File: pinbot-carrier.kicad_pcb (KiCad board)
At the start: 2 copper layers, 150 x 30 mm, 118 parts, among them J1 USB4105-GF-A-120, J2 Conn_02x20_Odd_Even, J3 HC-1.0-4PWT, J4 SM06B-SRSS-TB, J5 USB_A, J6 USB_A, J7 USB_A, K1 EC2-5SNU, K2 EC2-5SNU, K3 EC2-5SNU, K4 EC2-5SNU, U1 TCA9535PWR, U10 ZXBM5210-S, U11 ZXBM5210-S, U12 ZXBM5210-S, U13 MIC2026-2xM, U14 USBLC6-2SC6, U15 USBLC6-2SC6, U16 USBLC6-2SC6, U17 USBLC6-2SC6, U18 FE1.1s, U19 MIC2026-2xM, U2 ADS1015IDGS, U7 ADS1015IDGS, U8 74HC04, U9 ZXBM5210-S, Y1 12MHz

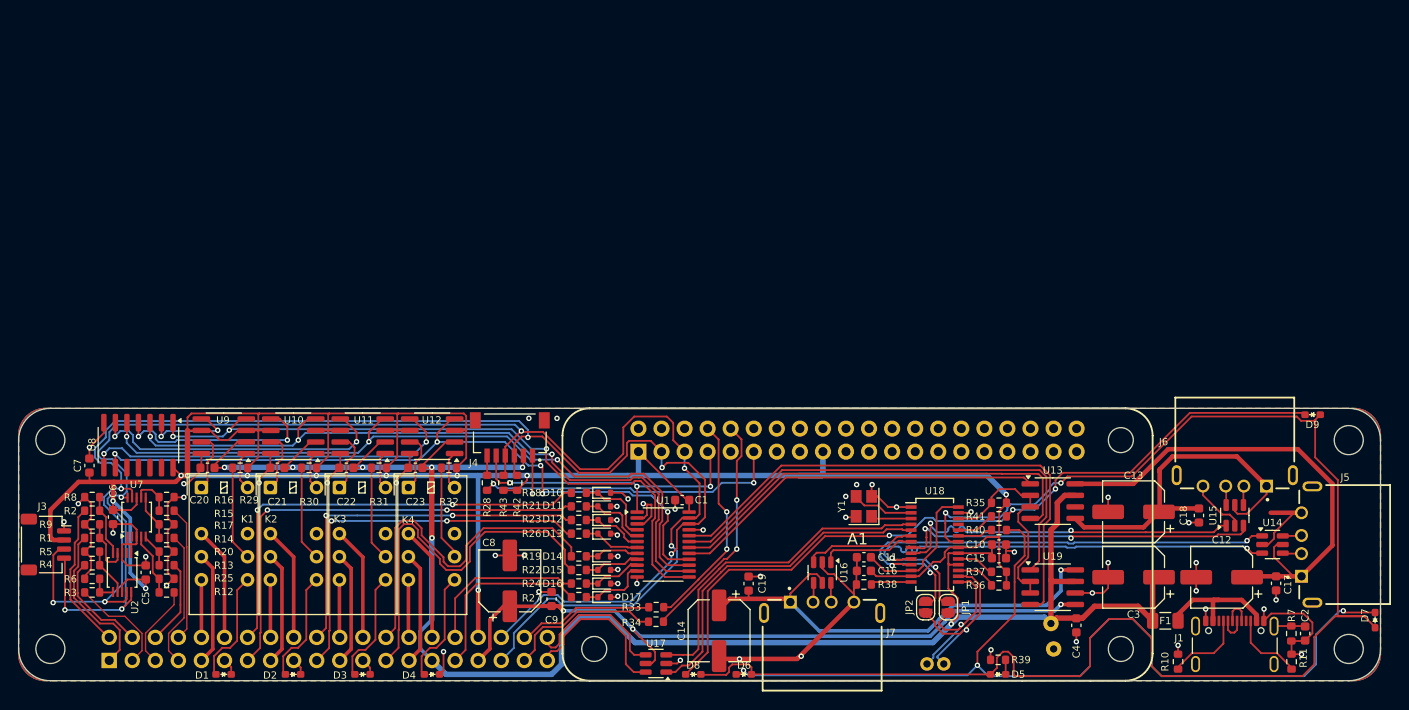
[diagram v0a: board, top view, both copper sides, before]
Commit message: r0.2 remade from a scratch
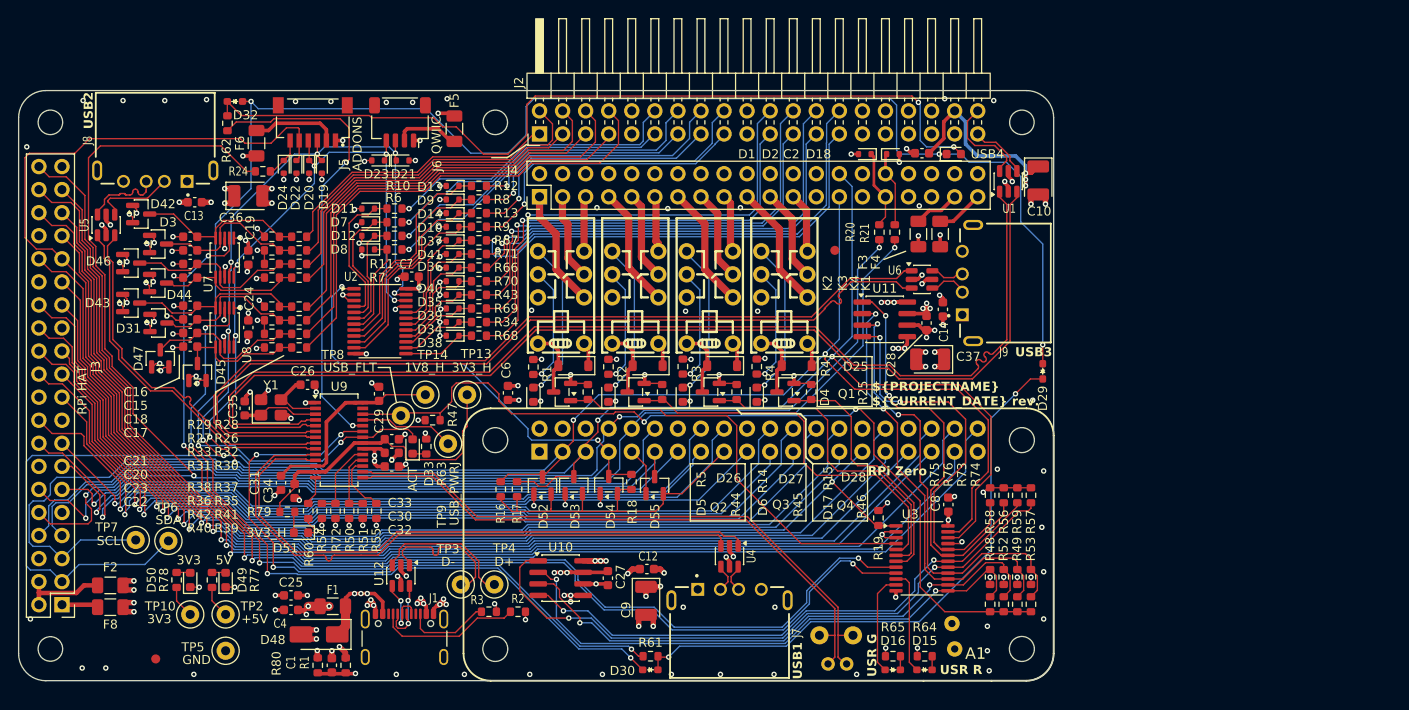
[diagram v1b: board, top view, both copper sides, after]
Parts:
- removed C11: 10uFx10V, Capacitor_SMD:C_0603_1608Metric
- removed the C13 at (122.8, -18.6)
- removed the C14 at (77.2, -5.50)
- removed C3: 100uFx16V, Capacitor_SMD:CP_Elec_6.3x5.4
- removed C5: 0.1uFx50V, Capacitor_SMD:C_0603_1608Metric
- removed the C7 at (7.80, -23.7)
- removed the C9 at (58.7, -9.00)
- removed JP1, JP2: SolderJumper_2_Open, Jumper:SolderJumper-2_P1.3mm_Open_RoundedPad1.0x1.5mm
- removed the R1 at (8.10, -15.7)
- removed the R16 at (16.3, -20.2)
- removed the R17 at (16.3, -17.2)
- removed the R2 at (8.10, -18.7)
- removed the R20 at (16.3, -14.2)
- removed the R21 at (61.7, -19.2)
- removed R22, R23: 10k, Resistor_SMD:R_0603_1608Metric
- removed the R24 at (61.7, -10.7)
- removed the R3 at (8.10, -9.72)
- removed U13, U19: MIC2026-2xM, Package_SO:SOIC-8_3.9x4.9mm_P1.27mm
- removed U18: FE1.1s, Package_SO:SSOP-28_3.9x9.9mm_P0.635mm
- removed the U2 at (11.4, -11.9)
- added C17: 0.1uFx50V, Capacitor_SMD:C_0603_1608Metric, F.Cu at (18.9, -44.4)
- added C18: 0.1uFx50V, Capacitor_SMD:C_0603_1608Metric, F.Cu at (18.9, -45.9)
- added C19: 0.1uFx50V, Capacitor_SMD:C_0603_1608Metric, F.Cu at (25.3, -46.6)
- added C2: 0.1uFx50V, Capacitor_SMD:C_0603_1608Metric, F.Cu at (99.5, -58.1)
- added C24: 0.1uFx50V, Capacitor_SMD:C_0603_1608Metric, F.Cu at (25.3, -38.9)
- added C25: 10uFx10V, Capacitor_SMD:C_0603_1608Metric, F.Cu at (30.0, -9.40)
- added C26: 14pFx50V, Capacitor_SMD:C_0603_1608Metric, F.Cu at (31.8, -32.6)
- added C27: 0.1uFx50V, Capacitor_SMD:C_0603_1608Metric, F.Cu at (64.9, -11.3)
- added C28: 0.1uFx50V, Capacitor_SMD:C_0603_1608Metric, F.Cu at (100.0, -39.4)
- added C29: 0.1uFx50V, Capacitor_SMD:C_0603_1608Metric, F.Cu at (39.7, -31.6)
- added C30: 0.1uFx50V, Capacitor_SMD:C_0603_1608Metric, F.Cu at (41.1, -25.1)
- added C31: 10uFx10V, Capacitor_SMD:C_0603_1608Metric, F.Cu at (28.9, -21.8)
- added C32: 10uFx10V, Capacitor_SMD:C_0603_1608Metric, F.Cu at (41.1, -23.6)
- added C33: 10uFx10V, Capacitor_SMD:C_0603_1608Metric, F.Cu at (41.1, -26.6)
- added C34: 0.1uFx50V, Capacitor_SMD:C_0603_1608Metric, F.Cu at (30.4, -20.9)
- added C35: 14pFx50V, Capacitor_SMD:C_0603_1608Metric, F.Cu at (24.9, -30.0)
- added C36: 100uFx10V, Capacitor_Tantalum_SMD:CP_EIA-3528-21_Kemet-B, F.Cu at (25.3, -53.4)
- added C37: 100uFx10V, Capacitor_Tantalum_SMD:CP_EIA-3528-21_Kemet-B, F.Cu at (100.4, -35.4)
- added D18: 19-21/GHC-YR1S2/4T, LED_SMD:LED_0603_1608Metric, F.Cu at (103.0, -58.0)
- added D19: ESD5Z3.3T5G, Diode_SMD:D_SOD-523, F.Cu at (33.4, -56.6)
- added D20: ESD5Z3.3T5G, Diode_SMD:D_SOD-523, F.Cu at (32.0, -56.6)
- added D21: ESD5Z3.3T5G, Diode_SMD:D_SOD-523, F.Cu at (42.3, -57.3)
- added D22: ESD5Z3.3T5G, Diode_SMD:D_SOD-523, F.Cu at (30.6, -56.6)
- added D23: ESD5Z3.3T5G, Diode_SMD:D_SOD-523, F.Cu at (39.6, -57.3)
- added D24: ESD5Z3.3T5G, Diode_SMD:D_SOD-523, F.Cu at (29.2, -56.6)
- added D25: MMSD4148, Diode_SMD:D_SOD-123, F.Cu at (85.7, -34.7)
- added D26: MMSD4148, Diode_SMD:D_SOD-123, F.Cu at (61.1, -34.7)
- added D27: MMSD4148, Diode_SMD:D_SOD-123, F.Cu at (69.3, -34.7)
- added D28: MMSD4148, Diode_SMD:D_SOD-123, F.Cu at (77.5, -34.7)
- added D29: LTST-S270KGKT, LED_0603_1608Metric_side:LED_0603_1608Metric_side, F.Cu at (112.8, -34.1)
- added D30: LTST-S270KGKT, LED_0603_1608Metric_side:LED_0603_1608Metric_side, F.Cu at (69.6, -1.20)
- added D31: BAT54S, Package_TO_SOT_SMD:SOT-23, F.Cu at (15.4, -39.4)
- added D32: LTST-S270KGKT, LED_0603_1608Metric_side:LED_0603_1608Metric_side, F.Cu at (23.8, -63.8)
- added D33: XL-1608SURC-06, LED_SMD:LED_0603_1608Metric, F.Cu at (43.4, -25.8)
- added D34: ESD5Z3.3T5G, Diode_SMD:D_SOD-523, F.Cu at (47.8, -39.5)
- added D35: ESD5Z3.3T5G, Diode_SMD:D_SOD-523, F.Cu at (47.8, -42.5)
- added D36: ESD5Z3.3T5G, Diode_SMD:D_SOD-523, F.Cu at (47.8, -45.5)
- added D37: ESD5Z3.3T5G, Diode_SMD:D_SOD-523, F.Cu at (47.8, -48.5)
- added D38: ESD5Z3.3T5G, Diode_SMD:D_SOD-523, F.Cu at (47.8, -38.0)
- added D39: ESD5Z3.3T5G, Diode_SMD:D_SOD-523, F.Cu at (47.8, -41.0)
- added D40: ESD5Z3.3T5G, Diode_SMD:D_SOD-523, F.Cu at (47.8, -44.0)
- added D41: ESD5Z3.3T5G, Diode_SMD:D_SOD-523, F.Cu at (47.8, -47.0)
- added D42: BAT54S, Package_TO_SOT_SMD:SOT-23, F.Cu at (13.5, -51.4)
- added D43: BAT54S, Package_TO_SOT_SMD:SOT-23, F.Cu at (12.4, -41.6)
- added D44: BAT54S, Package_TO_SOT_SMD:SOT-23, F.Cu at (15.4, -43.8)
- added D45: BAT54S, Package_TO_SOT_SMD:SOT-23, F.Cu at (19.7, -34.0)
- added D46: BAT54S, Package_TO_SOT_SMD:SOT-23, F.Cu at (12.4, -46.0)
- added D47: BAT54S, Package_TO_SOT_SMD:SOT-23, F.Cu at (15.6, -35.5)
- added D48: SMAJ5.0A, Diode_SMD:D_SMA, F.Cu at (33.1, -5.10)
- added D49: XL-1608SURC-06, LED_SMD:LED_0603_1608Metric, F.Cu at (22.8, -11.1)
- added D50: XL-1608SURC-06, LED_SMD:LED_0603_1608Metric, F.Cu at (18.9, -11.1)
- added D51: XL-1608SURC-06, LED_SMD:LED_0603_1608Metric, F.Cu at (31.1, -16.3)
- added D52: BAT54S, Package_TO_SOT_SMD:SOT-23, F.Cu at (57.7, -21.5)
- added D53: BAT54S, Package_TO_SOT_SMD:SOT-23, F.Cu at (61.1, -21.5)
- added D54: BAT54S, Package_TO_SOT_SMD:SOT-23, F.Cu at (65.0, -21.6)
- added D55: BAT54S, Package_TO_SOT_SMD:SOT-23, F.Cu at (70.0, -21.5)
- added F2: MF-NSMF110-2, Fuse:Fuse_1206_3216Metric, F.Cu at (10.1, -10.5)
- added F3: MF-NSMF110-2, Fuse:Fuse_1206_3216Metric, F.Cu at (99.1, -49.2)
- added F4: MF-NSMF110-2, Fuse:Fuse_1206_3216Metric, F.Cu at (101.5, -49.2)
- added F5: MF-NSMF110-2, Fuse:Fuse_1206_3216Metric, F.Cu at (48.0, -60.8)
- added F6: MF-NSMF110-2, Fuse:Fuse_1206_3216Metric, F.Cu at (26.2, -59.2)
- added F8: MF-NSMF110-2, Fuse:Fuse_1206_3216Metric, F.Cu at (10.1, -8.10)
- added FID1: Fiducial, Fiducial:Fiducial_1mm_Mask2mm, F.Cu at (15.1, -2.40)
- added FID2: Fiducial, Fiducial:Fiducial_1mm_Mask2mm, F.Cu at (89.9, -47.4)
- added J5: SM06B-SRSS-TB, SM06B-SRSS-TB:JST_SM06B-SRSS-TB, F.Cu at (32.4, -59.5)
- added J6: HC-1.0-4PWT, Connector_JST:JST_SH_SM04B-SRSS-TB_1x04-1MP_P1.00mm_Horizontal, F.Cu at (42.0, -61.5)
- added Q1: 2N7002, Package_TO_SOT_SMD:SOT-23, F.Cu at (84.5, -31.8)
- added Q2: 2N7002, Package_TO_SOT_SMD:SOT-23, F.Cu at (59.9, -31.8)
- added Q3: 2N7002, Package_TO_SOT_SMD:SOT-23, F.Cu at (68.0, -31.8)
- added Q4: 2N7002, Package_TO_SOT_SMD:SOT-23, F.Cu at (76.2, -31.8)
- added R10: 10k, Resistor_SMD:R_0603_1608Metric, F.Cu at (41.4, -52.0)
- added R11: 10k, Resistor_SMD:R_0603_1608Metric, F.Cu at (41.4, -49.0)
- added R28: 110k, Resistor_SMD:R_0603_1608Metric, F.Cu at (30.9, -48.9)
- added R33: 10k, Resistor_SMD:R_0603_1608Metric, F.Cu at (27.9, -45.9)
- added R34: 10k, Resistor_SMD:R_0603_1608Metric, F.Cu at (50.7, -39.5)
- added R42: 10k, Resistor_SMD:R_0603_1608Metric, F.Cu at (27.9, -38.2)
- added R43: 10k, Resistor_SMD:R_0603_1608Metric, F.Cu at (50.7, -42.5)
- added R44: 10k, Resistor_SMD:R_0603_1608Metric, F.Cu at (62.7, -31.8)
- added R45: 10k, Resistor_SMD:R_0603_1608Metric, F.Cu at (70.9, -31.8)
- added R46: 10k, Resistor_SMD:R_0603_1608Metric, F.Cu at (79.1, -31.8)
- added R47: 10k, Resistor_SMD:R_0603_1608Metric, F.Cu at (45.6, -28.7)
- added R48: 330R, Resistor_SMD:R_0603_1608Metric, F.Cu at (107.0, -8.43)
- added R49: 330R, Resistor_SMD:R_0603_1608Metric, F.Cu at (110.0, -8.43)
- added R50: 51k, Resistor_SMD:R_0603_1608Metric, F.Cu at (36.4, -18.7)
- added R51: 51k, Resistor_SMD:R_0603_1608Metric, F.Cu at (37.9, -18.7)
- added R52: 330R, Resistor_SMD:R_0603_1608Metric, F.Cu at (108.5, -8.43)
- added R53: 330R, Resistor_SMD:R_0603_1608Metric, F.Cu at (111.5, -8.43)
- added R54: 10k, Resistor_SMD:R_0603_1608Metric, F.Cu at (33.4, -18.7)
- added R55: 10k, Resistor_SMD:R_0603_1608Metric, F.Cu at (39.4, -18.7)
- added R56: 10k, Resistor_SMD:R_0603_1608Metric, F.Cu at (108.5, -11.4)
- added R57: 10k, Resistor_SMD:R_0603_1608Metric, F.Cu at (111.5, -11.4)
- added R58: 10k, Resistor_SMD:R_0603_1608Metric, F.Cu at (107.0, -11.4)
- added R59: 10k, Resistor_SMD:R_0603_1608Metric, F.Cu at (110.0, -11.4)
- added R60: 2.7k, Resistor_SMD:R_0603_1608Metric, F.Cu at (31.9, -18.7)
- added R61: 330R, Resistor_SMD:R_0603_1608Metric, F.Cu at (69.6, -2.70)
- added R62: 330R, Resistor_SMD:R_0603_1608Metric, F.Cu at (23.0, -61.4)
- added R63: 330R, Resistor_SMD:R_0603_1608Metric, F.Cu at (44.9, -25.8)
- added R64: 330R, Resistor_SMD:R_0603_1608Metric, F.Cu at (99.8, -2.70)
- added R65: 330R, Resistor_SMD:R_0603_1608Metric, F.Cu at (96.3, -2.70)
- added R66: 10k, Resistor_SMD:R_0603_1608Metric, F.Cu at (50.7, -45.5)
- added R67: 10k, Resistor_SMD:R_0603_1608Metric, F.Cu at (50.7, -48.5)
- added R68: 10k, Resistor_SMD:R_0603_1608Metric, F.Cu at (50.7, -38.0)
- added R69: 10k, Resistor_SMD:R_0603_1608Metric, F.Cu at (50.7, -41.0)
- added R7: 10k, Resistor_SMD:R_0603_1608Metric, F.Cu at (41.4, -47.5)
- added R70: 10k, Resistor_SMD:R_0603_1608Metric, F.Cu at (50.7, -44.0)
- added R71: 10k, Resistor_SMD:R_0603_1608Metric, F.Cu at (50.7, -47.0)
- added R72: 10k, Resistor_SMD:R_0603_1608Metric, F.Cu at (34.9, -18.7)
- added R73: 10k, Resistor_SMD:R_0603_1608Metric, F.Cu at (110.0, -20.4)
- added R74: 10k, Resistor_SMD:R_0603_1608Metric, F.Cu at (111.5, -20.4)
- added R75: 10k, Resistor_SMD:R_0603_1608Metric, F.Cu at (107.0, -20.4)
- added R76: 10k, Resistor_SMD:R_0603_1608Metric, F.Cu at (108.5, -20.4)
- added R77: 330R, Resistor_SMD:R_0603_1608Metric, F.Cu at (21.3, -11.1)
- added R78: 330R, Resistor_SMD:R_0603_1608Metric, F.Cu at (17.4, -11.1)
- added R79: 330R, Resistor_SMD:R_0603_1608Metric, F.Cu at (29.6, -18.6)
- added R80: 0, Resistor_SMD:R_0603_1608Metric, F.Cu at (32.9, -1.70)
- added TP10: 3V3, JLCImport:TestPoint_Loop_D1.80mm_Drill1.0mm_Beaded, F.Cu at (18.9, -7.30)
- added TP11: RPI_D+, JLCImport:TestPoint_Loop_D1.80mm_Drill1.0mm_Beaded, B.Cu at (91.9, -5.00)
- added TP12: RPI_D-, JLCImport:TestPoint_Loop_D1.80mm_Drill1.0mm_Beaded, B.Cu at (88.2, -5.00)
- added TP13: 3V3_H, JLCImport:TestPoint_Loop_D1.80mm_Drill1.0mm_Beaded, F.Cu at (49.4, -31.5)
- added TP14: 1V8_H, JLCImport:TestPoint_Loop_D1.80mm_Drill1.0mm_Beaded, F.Cu at (44.8, -31.5)
- added TP2: +5V, JLCImport:TestPoint_Loop_D1.80mm_Drill1.0mm_Beaded, F.Cu at (22.8, -7.30)
- added TP3: D-, JLCImport:TestPoint_Loop_D1.80mm_Drill1.0mm_Beaded, F.Cu at (48.7, -10.6)
- added TP4: D+, JLCImport:TestPoint_Loop_D1.80mm_Drill1.0mm_Beaded, F.Cu at (52.4, -10.6)
- added TP5: GND, JLCImport:TestPoint_Loop_D1.80mm_Drill1.0mm_Beaded, F.Cu at (22.8, -3.30)
- added TP6: SDA, JLCImport:TestPoint_Loop_D1.80mm_Drill1.0mm_Beaded, F.Cu at (16.5, -15.4)
- added TP7: SCL, JLCImport:TestPoint_Loop_D1.80mm_Drill1.0mm_Beaded, F.Cu at (12.9, -15.5)
- added TP8: USB_FLT, JLCImport:TestPoint_Loop_D1.80mm_Drill1.0mm_Beaded, F.Cu at (42.1, -29.2)
- added TP9: USB_PWRJ, JLCImport:TestPoint_Loop_D1.80mm_Drill1.0mm_Beaded, F.Cu at (47.3, -26.1)
- added U3: TCA9535PWR, Package_SO:TSSOP-24_4.4x7.8mm_P0.65mm, F.Cu at (99.5, -13.5)
- C10: value 0.1uFx50V -> 100uFx10V; footprint Capacitor_SMD:C_0603_1608Metric -> Capacitor_Tantalum_SMD:CP_EIA-3528-21_Kemet-B
- C15, C16: value 10uFx10V -> 0.1uFx50V
- C6: value 0.1uFx50V -> 10uFx10V
- C8: value 100uFx16V -> 0.1uFx50V; footprint Capacitor_SMD:CP_Elec_6.3x5.4 -> Capacitor_SMD:C_0603_1608Metric
- C9: renamed from C12; value 100uFx16V -> 100uFx10V; footprint Capacitor_SMD:CP_Elec_6.3x5.4 -> Capacitor_Tantalum_SMD:CP_EIA-3528-21_Kemet-B
- D1, D2, D7, D8, D9: value LTST-S270KGKT -> ESD5Z3.3T5G; footprint LED_0603_1608Metric_side:LED_0603_1608Metric_side -> Diode_SMD:D_SOD-523
- D15: value ESD5Z3.3T5G -> LTST-S270KRKT; footprint Diode_SMD:D_SOD-523 -> LED_0603_1608Metric_side:LED_0603_1608Metric_side
- D16: value ESD5Z3.3T5G -> LTST-S270KGKT; footprint Diode_SMD:D_SOD-523 -> LED_0603_1608Metric_side:LED_0603_1608Metric_side
- D17: value ESD5Z3.3T5G -> 19-21/GHC-YR1S2/4T; footprint Diode_SMD:D_SOD-523 -> LED_SMD:LED_0603_1608Metric
- D3: value LTST-S270KGKT -> BAT54S; footprint LED_0603_1608Metric_side:LED_0603_1608Metric_side -> Package_TO_SOT_SMD:SOT-23
- D4, D6: value LTST-S270KGKT -> 19-21/GHC-YR1S2/4T; footprint LED_0603_1608Metric_side:LED_0603_1608Metric_side -> LED_SMD:LED_0603_1608Metric
- D5: value LTST-S270KRKT -> 19-21/GHC-YR1S2/4T; footprint LED_0603_1608Metric_side:LED_0603_1608Metric_side -> LED_SMD:LED_0603_1608Metric
- H1, H2, H3, H4: footprint MountingHoles:MountingHole_3.2mm_M3_keepouts -> JLCImport:MountingHole_2.7mm
- J2: footprint Connector_PinSocket_2.54mm:PinSocket_2x20_P2.54mm_Vertical -> Connector_PinHeader_2.54mm:PinHeader_2x20_P2.54mm_Horizontal; moved to F.Cu
- J3: value HC-1.0-4PWT -> Raspberry_Pi_4; footprint Connector_JST:JST_SH_SM04B-SRSS-TB_1x04-1MP_P1.00mm_Horizontal -> Connector_PinHeader_2.54mm:PinHeader_2x20_P2.54mm_Vertical
- J4: value SM06B-SRSS-TB -> Conn_02x20_Odd_Even; footprint SM06B-SRSS-TB:JST_SM06B-SRSS-TB -> Connector_PinHeader_2.54mm:PinHeader_2x20_P2.54mm_Vertical
- K1, K2, K3, K4: value EC2-5SNU -> G6S-2-5V; footprint Relay_THT:Relay_DPDT_Kemet_EC2 -> JLCImport:G6S-2-5V
- R12, R13: value 820k -> 10k
- R14, R15, R4: value 820k -> 330R
- R25, R6, R8, R9: value 120k -> 10k
- R26, R35, R37: value 10k -> 110k
- R29, R31, R40: value 330R -> 10k
- R30, R32, R39, R41: value 330R -> 110k
- R38: value 2.7k -> 10k
- R5: value 120k -> 330R
- U10, U11: value ZXBM5210-S -> MIC2026-2xM
- U12: value ZXBM5210-S -> USBLC6-2SC6; footprint Package_SO:SOIC-8_3.9x4.9mm_P1.27mm -> Package_TO_SOT_SMD:SOT-23-6
- U8: value 74HC04 -> ADS1015IDGS; footprint Package_SO:SOIC-14_3.9x8.7mm_P1.27mm -> Package_SO:TSSOP-10_3x3mm_P0.5mm
- U9: value ZXBM5210-S -> FE1.1s; footprint Package_SO:SOIC-8_3.9x4.9mm_P1.27mm -> Package_SO:SSOP-28_3.9x9.9mm_P0.635mm
- moved U5 128.4 mm to (9.64, -50.2)
- moved J8 123.5 mm to (15.1, -56.2)
- moved D7 119.2 mm to (38.5, -50.5), turned to 180 degrees
- moved C13 115.9 mm to (19.4, -52.7), turned to 180 degrees
- moved H3 110.5 mm to (52.5, -61.5)
- moved C1 107.3 mm to (34.5, -1.70), turned to -90 degrees
- moved R1 104.2 mm to (36.0, -1.70), turned to 90 degrees
- moved D9 97.6 mm to (47.8, -53.0), turned to 180 degrees
- moved C15 95.3 mm to (18.9, -47.4), turned to 0 degrees
- moved F1 91.7 mm to (34.6, -8.20)
- moved J1 91.5 mm to (42.5, -3.69)
- moved D1 90.9 mm to (93.2, -58.0)
- moved R3 88.6 mm to (51.8, -7.60), turned to 0 degrees
- moved D2 87.4 mm to (96.3, -58.0), turned to 0 degrees
- moved C4 86.5 mm to (30.0, -7.80), turned to 0 degrees
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- renumbered C2 to C1, C17 to C12, C18 to C13, C19 to C14, C1 to C7, J5 to J7, J6 to J8, J7 to J9, R7 to R1, R42 to R16, R43 to R17, R10 to R2, R33 to R20, R34 to R21, R28 to R24, R11 to R3, U17 to U1, U1 to U2, U14 to U4, U15 to U5, U16 to U6
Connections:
- net Net-(J5-D+) renamed /O1D+
- net Net-(J5-D-) renamed /O1D-
- net Net-(J6-D+) renamed /O2D+
- net Net-(J6-D-) renamed /O2D-
- net Net-(J7-D+) renamed /O3D+
- net Net-(J7-D-) renamed /O3D-
- A1 pad 10: Net-(A1-GP15/RXD) -> /RPi_GPIO15
- A1 pad 12: unconnected-(A1-GP18-Pad12) -> /RPi_GPIO18
- A1 pad 13: unconnected-(A1-GP27-Pad13) -> /RPi_GPIO27
- A1 pad 15: unconnected-(A1-GP22-Pad15) -> /RPi_GPIO22
- A1 pad 16: unconnected-(A1-GP23-Pad16) -> /RPi_GPIO23
- A1 pad 18: unconnected-(A1-GP24-Pad18) -> /RPi_GPIO24
- A1 pad 19: unconnected-(A1-GP10/MOSI-Pad19) -> /RPi_GPIO10
- A1 pad 2: unconnected-(A1-+5V-Pad2) -> +5V
- A1 pad 21: unconnected-(A1-GP9/MISO-Pad21) -> /RPi_GPIO9
- A1 pad 22: unconnected-(A1-GP25-Pad22) -> /RPi_GPIO25
- A1 pad 23: unconnected-(A1-GP11/SCLK-Pad23) -> /RPi_GPIO11
- A1 pad 24: unconnected-(A1-GP8/CS0-Pad24) -> /RPi_GPIO8
- A1 pad 26: unconnected-(A1-GP7/CS1-Pad26) -> /RPi_GPIO7
- A1 pad 27: unconnected-(A1-GP0-Pad27) -> /RPi_GPIO0
- A1 pad 28: unconnected-(A1-GP1-Pad28) -> /RPi_GPIO1
- A1 pad 29: unconnected-(A1-GP5-Pad29) -> /RPi_GPIO5
- A1 pad 3: /SDA -> /RPi_GPIO2
- A1 pad 31: unconnected-(A1-GP6-Pad31) -> /RPi_GPIO6
- A1 pad 32: unconnected-(A1-GP12/PWM0-Pad32) -> /RPi_GPIO12
- A1 pad 33: unconnected-(A1-GP13/PWM1-Pad33) -> /RPi_GPIO13
- A1 pad 35: unconnected-(A1-GP19-Pad35) -> /RPi_GPIO19
- A1 pad 36: unconnected-(A1-GP16-Pad36) -> /RPi_GPIO16
- A1 pad 37: unconnected-(A1-GP26-Pad37) -> /RPi_GPIO26
- A1 pad 38: unconnected-(A1-GP20-Pad38) -> /RPi_GPIO20
- A1 pad 4: unconnected-(A1-+5V-Pad4) -> +5V
- A1 pad 40: unconnected-(A1-GP21-Pad40) -> /RPi_GPIO21
- A1 pad 5: /SCL -> /RPi_GPIO3
- A1 pad 7: /~{INT} -> /RPi_GPIO4
- A1 pad 8: Net-(A1-GP14/TXD) -> /RPi_GPIO14
- C10 pad 1: GND -> +5V_USB4
- C10 pad 2: +5V -> GND
- C15 pad 2: +5V -> /ADC0/ANF0
- C16 pad 2: +3V3 -> /ADC0/ANF1
- C20 pad 2: +5V -> /ADC1/ANF0
- C21 pad 2: +5V -> /ADC1/ANF1
- C22 pad 2: +5V -> /ADC1/ANF2
- C23 pad 2: +5V -> /ADC1/ANF3
- C6 pad 2: +3V3 -> +5V
- C8 pad 1: +5V_USB4 -> GND
- C8 pad 2: GND -> +3V3
- D1 pad 1: GND -> /TXD_OUT
- D1 pad 2: Net-(D1-A) -> GND
- D10 pad 1: /GPIO0 -> /GPIO7
- D11 pad 1: /GPIO1 -> /GPIO0
- D13 pad 1: /GPIO3 -> /GPIO4
- D14 pad 1: /GPIO4 -> /GPIO6
- D15 pad 1: /GPIO5 -> Net-(D15-K)
- D15 pad 2: GND -> Net-(D15-A)
- D16 pad 1: /GPIO6 -> Net-(D16-K)
- D16 pad 2: GND -> Net-(D16-A)
- D17 pad 1: /GPIO7 -> GND
- D17 pad 2: GND -> /RELAY3/NO2
- D2 pad 1: GND -> /RXD_OUT
- D2 pad 2: Net-(D2-A) -> GND
- D3 pad 2: Net-(D3-A) -> +3V3
- D4 pad 2: Net-(D4-A) -> /RELAY4/NO2
- D5 pad 1: Net-(D5-K) -> GND
- D5 pad 2: Net-(D5-A) -> /RELAY1/NO2
- D6 pad 1: Net-(D5-A) -> GND
- D6 pad 2: Net-(D6-A) -> /RELAY2/NO2
- D7 pad 1: Net-(D6-A) -> /GPIO1
- D7 pad 2: Net-(D5-A) -> GND
- D8 pad 1: Net-(D5-A) -> /GPIO3
- D8 pad 2: Net-(D8-A) -> GND
- D9 pad 1: Net-(D8-A) -> /GPIO5
- D9 pad 2: Net-(D5-A) -> GND
- J1 pad A6: /USB_D+ -> Net-(J1-D+-PadA6)
- J1 pad A7: /USB_D- -> Net-(J1-D--PadA7)
- J1 pad B6: /USB_D+ -> Net-(J1-D+-PadA6)
- J1 pad B7: /USB_D- -> Net-(J1-D--PadA7)
- J2 pad 1: /AN0 -> /AN1
- J2 pad 10: /NO1 -> GND
- J2 pad 11: GND -> /GPIO1_OUT
- J2 pad 12: /NC1 -> /GPIO0_OUT
- J2 pad 13: /GPIO1_OUT -> /GPIO3_OUT
- J2 pad 14: /GPIO0_OUT -> /GPIO2_OUT
- J2 pad 15: /COM2 -> /GPIO5_OUT
- J2 pad 16: /NO2 -> /GPIO4_OUT
- J2 pad 17: GND -> /GPIO7_OUT
- J2 pad 18: /NC2 -> /GPIO6_OUT
- J2 pad 19: /GPIO3_OUT -> GND
- J2 pad 2: /AN1 -> /AN0
- J2 pad 20: /GPIO2_OUT -> GND
- J2 pad 21: /COM3 -> /GPIO9_OUT
- J2 pad 22: /NO3 -> /GPIO8_OUT
- J2 pad 23: GND -> /GPIO11_OUT
- J2 pad 24: /NC3 -> /GPIO10_OUT
- J2 pad 25: /GPIO5_OUT -> /GPIO13_OUT
- J2 pad 26: /GPIO4_OUT -> /GPIO12_OUT
- J2 pad 27: /COM4 -> /GPIO15_OUT
- J2 pad 28: /NO4 -> /GPIO14_OUT
- J2 pad 29: +5V -> unconnected-(J2-Pin_29-Pad29)
- J2 pad 3: /AN2 -> /AN3
- J2 pad 30: /NC4 -> unconnected-(J2-Pin_30-Pad30)
- J2 pad 31: /GPIO7_OUT -> unconnected-(J2-Pin_31-Pad31)
- J2 pad 32: /GPIO6_OUT -> unconnected-(J2-Pin_32-Pad32)
- J2 pad 33: +5V_USB4 -> unconnected-(J2-Pin_33-Pad33)
- J2 pad 34: +3V3 -> unconnected-(J2-Pin_34-Pad34)
- J2 pad 35: /SCL -> GND
- J2 pad 36: /SDA -> GND
- J2 pad 37: /RXD_OUT -> GND
- J2 pad 38: /TXD_OUT -> +5V_USB4
- J2 pad 39: /4O_D+ -> /4O_D-
- J2 pad 4: /AN3 -> /AN2
- J2 pad 40: /4O_D- -> /4O_D+
- J2 pad 5: /AN4 -> /AN5
- J2 pad 6: /AN5 -> /AN4
- J2 pad 7: /AN6 -> /AN7
- J2 pad 8: /AN7 -> /AN6
- J2 pad 9: /COM1 -> GND
- J3 pad 1: GND -> Net-(F8-Pad1)
- J3 pad 2: +3V3 -> Net-(F2-Pad1)
- J3 pad 3: /SDA -> /RPi_GPIO2
- J3 pad 4: /SCL -> Net-(F2-Pad1)
- J4 pad 1: GND -> /R_NC1
- J4 pad 2: +5V -> unconnected-(J4-Pin_2-Pad2)
- J4 pad 3: /SDA -> /R_COM1
- J4 pad 4: /SCL -> GND
- J4 pad 5: /~{INT} -> /R_NO1
- J4 pad 6: Net-(J4-Pin_6) -> unconnected-(J4-Pin_6-Pad6)
- J7 pad 5: unconnected-(J5-Shield-Pad5) -> GND
- J8 pad 5: unconnected-(J6-Shield-Pad5) -> GND
- J9 pad 5: unconnected-(J7-Shield-Pad5) -> GND
- K1 pad 1: Net-(U9-OUT2) -> +5V
- K1 pad 10: unconnected-(K1-Pad10) -> /RELAY4/NC2
- K1 pad 12: Net-(U9-OUT1) -> Net-(D25-A)
- K1 pad 3: /NC1 -> /R_NC4
- K1 pad 4: /COM1 -> /R_COM4
- K1 pad 5: /NO1 -> /R_NO4
- K1 pad 8: Net-(D1-A) -> /RELAY4/NO2
- K1 pad 9: Net-(K1-Pad9) -> /RELAY4/COM2
- K2 pad 1: Net-(U10-OUT2) -> +5V
- K2 pad 10: unconnected-(K2-Pad10) -> /RELAY1/NC2
- K2 pad 12: Net-(U10-OUT1) -> Net-(D26-A)
- K2 pad 3: /NC2 -> /R_NC1
- K2 pad 4: /COM2 -> /R_COM1
- K2 pad 5: /NO2 -> /R_NO1
- K2 pad 8: Net-(D2-A) -> /RELAY1/NO2
- K2 pad 9: Net-(K2-Pad9) -> /RELAY1/COM2
- K3 pad 1: Net-(U11-OUT2) -> +5V
- K3 pad 10: unconnected-(K3-Pad10) -> /RELAY2/NC2
- K3 pad 12: Net-(U11-OUT1) -> Net-(D27-A)
- K3 pad 3: /NC3 -> /R_NC2
- K3 pad 4: /COM3 -> /R_COM2
- K3 pad 5: /NO3 -> /R_NO2
- K3 pad 8: Net-(D3-A) -> /RELAY2/NO2
- K3 pad 9: Net-(K3-Pad9) -> /RELAY2/COM2
- K4 pad 1: Net-(U12-OUT2) -> +5V
- K4 pad 10: unconnected-(K4-Pad10) -> /RELAY3/NC2
- K4 pad 12: Net-(U12-OUT1) -> Net-(D28-A)
- K4 pad 3: /NC4 -> /R_NC3
- K4 pad 4: /COM4 -> /R_COM3
- K4 pad 5: /NO4 -> /R_NO3
- K4 pad 8: Net-(D4-A) -> /RELAY3/NO2
- K4 pad 9: Net-(K4-Pad9) -> /RELAY3/COM2
- R12 pad 1: /AN4 -> /GPIO4
- R12 pad 2: Net-(U7-AIN0) -> /GPIO4_OUT
- R13 pad 1: /AN5 -> /GPIO6
- R13 pad 2: Net-(U7-AIN1) -> /GPIO6_OUT
- R14 pad 1: /AN6 -> +5V
- R14 pad 2: Net-(U7-AIN2) -> /RELAY2/COM2
- R15 pad 1: /AN7 -> +5V
- R15 pad 2: Net-(U7-AIN3) -> /RELAY3/COM2
- R16 pad 2: /SDA -> /RPi_GPIO2
- R17 pad 2: /SCL -> /RPi_GPIO3
- R18 pad 1: /GPIO0 -> +3V3
- R18 pad 2: /GPIO0_OUT -> /RPi_GPIO4
- R19 pad 1: /GPIO4 -> +3V3
- R19 pad 2: /GPIO4_OUT -> /RPi_GPIO5
- R20 pad 2: Net-(A1-GP14/TXD) -> /RPi_GPIO14
- R21 pad 2: Net-(A1-GP15/RXD) -> /RPi_GPIO15
- R24 pad 1: Net-(J4-Pin_6) -> Net-(D24-K)
- R25 pad 1: Net-(U7-AIN0) -> GND
- R25 pad 2: GND -> /RELAY4
- R26 pad 1: /GPIO3 -> /AN0
- R26 pad 2: /GPIO3_OUT -> /ADC0/ANF0
- R27 pad 1: /GPIO7 -> GND
- R27 pad 2: /GPIO7_OUT -> /ADC0/ANF0
- R29 pad 1: +3V3 -> GND
- R29 pad 2: Net-(K1-Pad9) -> /ADC0/ANF1
- R30 pad 1: Net-(K2-Pad9) -> /AN2
- R30 pad 2: +3V3 -> /ADC0/ANF2
- R31 pad 1: Net-(K3-Pad9) -> GND
- R31 pad 2: +3V3 -> /ADC0/ANF2
- R32 pad 1: Net-(K4-Pad9) -> /AN3
- R32 pad 2: +3V3 -> /ADC0/ANF3
- R35 pad 1: +3V3 -> /AN4
- R35 pad 2: /USB_FLT -> /ADC1/ANF0
- R36 pad 1: +3V3 -> GND
- R36 pad 2: Net-(U18-~{XRSTJ}) -> /ADC1/ANF0
- R37 pad 1: +3V3 -> /AN5
- R37 pad 2: Net-(U18-BUSJ) -> /ADC1/ANF1
- R38 pad 2: Net-(U18-REXT) -> /ADC1/ANF1
- R39 pad 1: Net-(D5-K) -> /AN6
- R39 pad 2: GND -> /ADC1/ANF2
- R4 pad 1: /AN3 -> +5V
- R4 pad 2: Net-(U2-AIN3) -> /RELAY4/COM2
- R40 pad 1: Net-(D6-A) -> GND
- R40 pad 2: Net-(U18-LED1/EESCL) -> /ADC1/ANF2
- R41 pad 1: Net-(D8-A) -> /AN7
- R41 pad 2: Net-(U18-LED2) -> /ADC1/ANF3
- R5 pad 1: Net-(U2-AIN3) -> +5V
- R5 pad 2: GND -> /RELAY1/COM2
- R6 pad 1: Net-(U2-AIN2) -> /GPIO1
- R6 pad 2: GND -> /GPIO1_OUT
- R8 pad 1: Net-(U2-AIN1) -> /GPIO5
- R8 pad 2: GND -> /GPIO5_OUT
- R9 pad 1: Net-(U2-AIN0) -> /GPIO7
- R9 pad 2: GND -> /GPIO7_OUT
- U10 pad 1: Net-(U10-OUT1) -> /USB_EN1
- U10 pad 2: +5V -> /USB_FLT1
- U10 pad 3: +3V3 -> /USB_FLT2
- U10 pad 4: /RELAY2 -> /USB_EN2
- U10 pad 5: /~{RELAY2} -> +5V_USB2
- U10 pad 6: +3V3 -> GND
- U10 pad 7: Net-(U10-OUT2) -> +5V
- U10 pad 8: GND -> +5V_USB1
- U11 pad 1: Net-(U11-OUT1) -> /USB_EN3
- U11 pad 2: +5V -> /USB_FLT3
- U11 pad 3: +3V3 -> /USB_FLT4
- U11 pad 4: /RELAY3 -> /USB_EN4
- U11 pad 5: /~{RELAY3} -> +5V_USB4
- U11 pad 6: +3V3 -> GND
- U11 pad 7: Net-(U11-OUT2) -> +5V
- U11 pad 8: GND -> +5V_USB3
- U12 pad 1: Net-(U12-OUT1) -> /USB_D-
- U12 pad 2: +5V -> GND
- U12 pad 3: +3V3 -> /USB_D+
- U12 pad 4: /RELAY4 -> Net-(J1-D+-PadA6)
- U12 pad 5: /~{RELAY4} -> +5V
- U12 pad 6: +3V3 -> Net-(J1-D--PadA7)
- U2 pad 1: /~{INT} -> /RPi_GPIO4
- U2 pad 13: /RELAY1 -> /GPIO8
- U2 pad 14: /RELAY2 -> /GPIO9
- U2 pad 15: /RELAY3 -> /GPIO10
- U2 pad 16: /RELAY4 -> /GPIO11
- U2 pad 17: /USB1_EN -> /GPIO12
- U2 pad 18: /USB2_EN -> /GPIO13
- U2 pad 19: /USB3_EN -> /GPIO14
- U2 pad 20: /USB4_EN -> /GPIO15
- U2 pad 22: /SDA -> /RPi_GPIO3
- U2 pad 23: /SCL -> /RPi_GPIO2
- U7 pad 10: /SCL -> /RPi_GPIO3
- U7 pad 2: unconnected-(U7-ALERT/RDY-Pad2) -> /ALERT0
- U7 pad 4: Net-(U7-AIN0) -> /ADC0/ANF0
- U7 pad 5: Net-(U7-AIN1) -> /ADC0/ANF1
- U7 pad 6: Net-(U7-AIN2) -> /ADC0/ANF2
- U7 pad 7: Net-(U7-AIN3) -> /ADC0/ANF3
- U7 pad 9: /SDA -> /RPi_GPIO2
- U8 pad 1: /RELAY1 -> +3V3
- U8 pad 10: (no net) -> /RPi_GPIO3
- U8 pad 2: /~{RELAY1} -> /ALERT1
- U8 pad 3: /RELAY2 -> GND
- U8 pad 4: /~{RELAY2} -> /ADC1/ANF0
- U8 pad 5: /RELAY3 -> /ADC1/ANF1
- U8 pad 6: /~{RELAY3} -> /ADC1/ANF2
- U8 pad 7: GND -> /ADC1/ANF3
- U8 pad 8: /~{RELAY4} -> +3V3
- U8 pad 9: /RELAY4 -> /RPi_GPIO2
- U9 pad 1: Net-(U9-OUT1) -> GND
- U9 pad 2: +5V -> Net-(U9-XOUT)
- U9 pad 3: +3V3 -> Net-(U9-XIN)
- U9 pad 4: /RELAY1 -> /4D-
- U9 pad 5: /~{RELAY1} -> /4D+
- U9 pad 6: +3V3 -> /3D-
- U9 pad 7: Net-(U9-OUT2) -> /3D+
- U9 pad 8: GND -> /2D-
- Y1 pad 1: Net-(U18-XIN) -> Net-(U9-XIN)
- Y1 pad 3: Net-(U18-XOUT) -> Net-(U9-XOUT)
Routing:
- net /RPi_GPIO2: track 0.00 -> 266.9 mm, vias 0 -> 9
- net /RPi_GPIO3: track 0.00 -> 257.3 mm, vias 0 -> 9
- net Net-(D18-K): track 0.00 -> 251.6 mm, vias 0 -> 7
- net +3V3: track 287.1 -> 91.8 mm, vias 11 -> 29
- net Net-(D5-A): track 170.5 -> 0.00 mm, vias 2 -> 0
- net /RPi_GPIO6: track 0.00 -> 166.7 mm, vias 0 -> 1
- net /SCL: track 158.8 -> 0.00 mm, vias 6 -> 0
- net /SDA: track 156.5 -> 0.00 mm, vias 6 -> 0
- net /RPi_GPIO21: track 0.00 -> 143.5 mm, vias 0 -> 1
- net /RPi_GPIO20: track 0.00 -> 137.5 mm, vias 0 -> 1
- net /RPi_GPIO26: track 0.00 -> 134.9 mm, vias 0 -> 1
- net /RPi_GPIO16: track 0.00 -> 131.1 mm, vias 0 -> 1
- net /RPi_GPIO19: track 0.00 -> 127.4 mm, vias 0 -> 1
- net /RPi_GPIO12: track 0.00 -> 122.6 mm, vias 0 -> 1
- net /RPi_GPIO5: track 0.00 -> 121.9 mm, vias 0 -> 2
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- added copper zone on In2.Cu, net +3V3
- added copper zone on In2.Cu, net +5V
- added copper zone on In2.Cu, net +5V_USB1
- added copper zone on In2.Cu, net +5V_USB2
- added copper zone on In1.Cu, net GND
- added copper zone on In2.Cu, net GND
- added copper zone on In2.Cu, net Net-(D48-A1)
- removed copper zone on B.Cu, net GND
- removed copper zone on F.Cu, net GND
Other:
- board size 150 x 30 mm -> 114 x 65 mm
- copper layers 2 -> 4
- board text added: "${PROJECTNAME} ${CURRENT_DATE} rev.${REVISION}"
- board text added: "3V3"
- board text added: "5V"
- board text added: "ADDONS"
- board text added: "Impedance Control: Yes Stackup: JLC04161H-3313 Finished thickness: 1.56 mm ±10% Target impedance: 90 Ω differential Layer: Top Reference: L2 GND"
- board text added: "QWIIC"
- board text added: "R1"
- board text added: "R2"
- board text added: "R3"
- board text added: "R4"
- board text added: "RPi HAT"
- board text added: "RPi Zero"
